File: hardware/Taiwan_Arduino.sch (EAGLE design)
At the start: 43 parts, among them J1 AVR_SPI_PRG_62X3_LOCK, T2 2N, U1 ATMEGA328P_PDIP, Y2 16mhz

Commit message: ver 1.0
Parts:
- removed R7: 1M, SparkFun-Resistors:RESISTORPTH-1/4W
- removed TP5: TEST-POINT, SparkFun-Passives:TEST-POINT
- added D3: 3.3V, _JJG-parts:DIODE-VERTDIODE_SM_VERT
- added JP1: Battery, SparkFun-Connectors:M02PTH
- C10, C13, C5, C8: device SparkFun-Capacitors:CAPPTH -> SparkFun-Capacitors:CAPPTH1
- C2: value 0.1uf -> 104; device SparkFun-Capacitors:CAPPTH -> SparkFun-Capacitors:CAPPTH1
- JP3: value M02JST-PTH-VERT -> M021X02_NO_SILK; device SparkFun-Connectors:M02JST-PTH-VERT -> SparkFun-Connectors:M021X02_NO_SILK
- R1: value (none) -> 10
- R9: device SparkFun-Resistors:RESISTORPTH-1/4W -> SparkFun-Resistors:RESISTORPTH-1/4W-VERT
- T2: value 2N -> 2N2222
- U2: value SPI_FLASH-X25XX -> SPI_FLASH
- renumbered U$1 to U2
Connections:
- removed net N$27: R7.2, TP5.1, U1.PD4(XCK/T0)
- new net N$18: D3.A, JP1.2
- net +5V: now also D3.C
- net GND: now also JP1.1
- net N$11: now also U1.PC3(ADC3); no longer R7.1, U1.PC2(ADC2)
- net N$28: now also U1.PB2(SS/OC1B); no longer U1.PB0(ICP)
- net N$3: now also U1.PB0(ICP); no longer U1.PB2(SS/OC1B)
- net N$5: now also U1.PC2(ADC2); no longer U1.PC1(ADC1)
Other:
- moved on the sheet: JP3, TP1, TP9

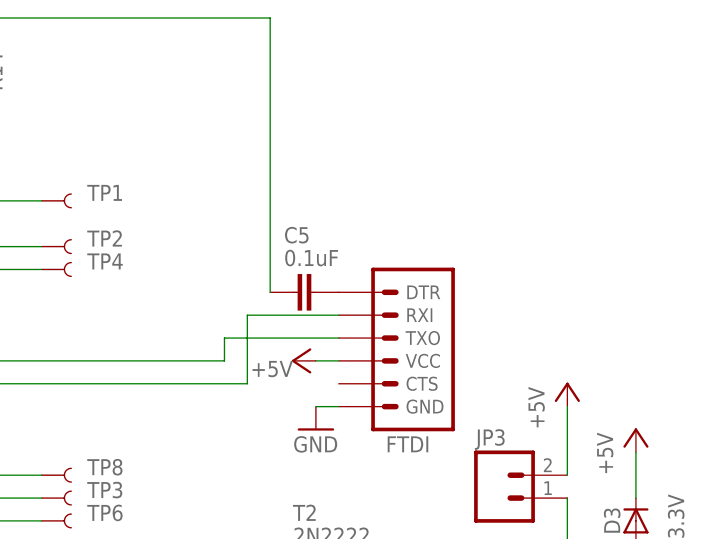
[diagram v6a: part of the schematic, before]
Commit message: add tag on FTDI port
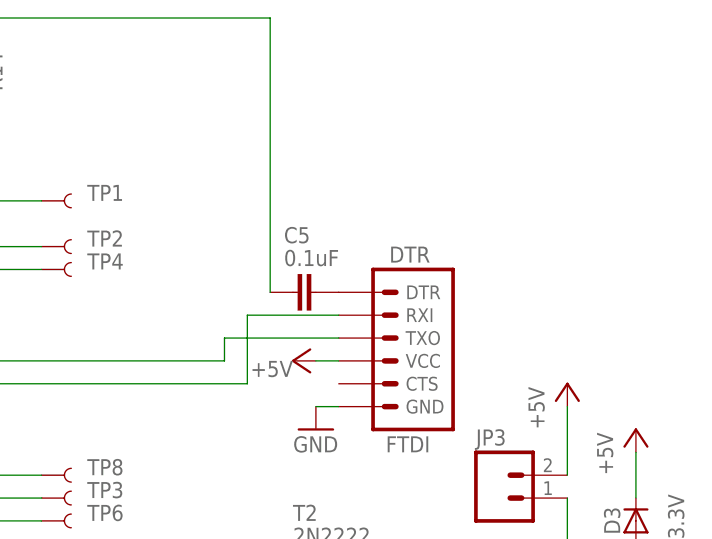
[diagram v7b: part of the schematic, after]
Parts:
- FTDI: value (none) -> DTR
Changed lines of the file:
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@@
 <part name="TP8" library="SparkFun-Passives" deviceset="TEST-POINT" device=""/>
 <part name="TP9" library="SparkFun-Passives" deviceset="TEST-POINT" device=""/>
-<part name="FTDI" library="SparkFun-Connectors" deviceset="ARDUINO_SERIAL_PROGRAM" device="LOCK"/>
+<part name="FTDI" library="SparkFun-Connectors" deviceset="ARDUINO_SERIAL_PROGRAM" device="LOCK" value="DTR"/>
 <part name="GND3" library="supply1" deviceset="GND" device=""/>
 <part name="P+1" library="supply1" deviceset="+5V" device=""/>

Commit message: add FTDI pin labels
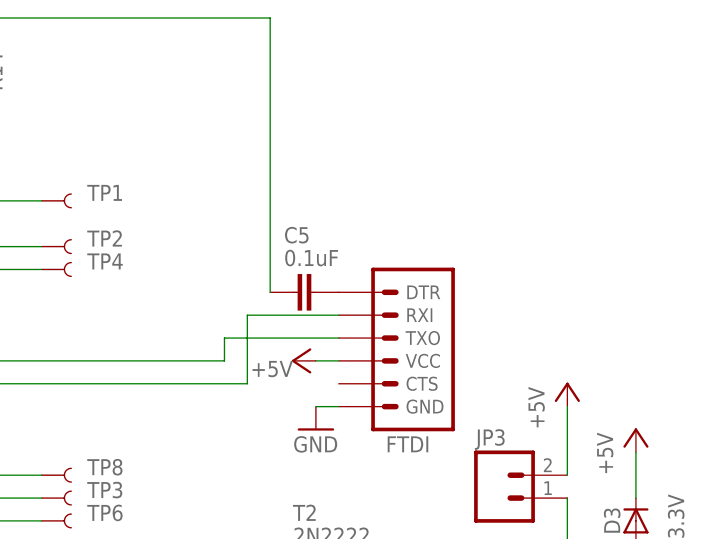
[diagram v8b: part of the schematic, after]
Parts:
- FTDI: value DTR -> (none)
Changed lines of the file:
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@@
 <?xml version="1.0" encoding="utf-8"?>
 <!DOCTYPE eagle SYSTEM "eagle.dtd">
-<eagle version="7.4.0">
+<eagle version="7.2.0">
 <drawing>
 <settings>
@@
 <grid distance="0.1" unitdist="inch" unit="inch" style="lines" multiple="1" display="no" altdistance="0.01" altunitdist="inch" altunit="inch"/>
 <layers>
-<layer number="1" name="Top" color="4" fill="1" visible="no" active="no"/>
-<layer number="16" name="Bottom" color="1" fill="1" visible="no" active="no"/>
-<layer number="17" name="Pads" color="2" fill="1" visible="no" active="no"/>
-<layer number="18" name="Vias" color="2" fill="1" visible="no" active="no"/>
-<layer number="19" name="Unrouted" color="6" fill="1" visible="no" active="no"/>
-<layer number="20" name="Dimension" color="15" fill="1" visible="no" active="no"/>
-<layer number="21" name="tPlace" color="7" fill="1" visible="no" active="no"/>
-<layer number="22" name="bPlace" color="7" fill="1" visible="no" active="no"/>
-<layer number="23" name="tOrigins" color="15" fill="1" visible="no" active="no"/>
-<layer number="24" name="bOrigins" color="15" fill="1" visible="no" active="no"/>
-<layer number="25" name="tNames" color="7" fill="1" visible="no" active="no"/>
-<layer number="26" name="bNames" color="7" fill="1" visible="no" active="no"/>
-<layer number="27" name="tValues" color="7" fill="1" visible="no" active="no"/>
-<layer number="28" name="bValues" color="7" fill="1" visible="no" active="no"/>
+<layer number="1" name="Top" color="4" fill="1" visible="yes" active="no"/>
+<layer number="16" name="Bottom" color="1" fill="1" visible="yes" active="no"/>
+<layer number="17" name="Pads" color="2" fill="1" visible="yes" active="no"/>
+<layer number="18" name="Vias" color="2" fill="1" visible="yes" active="no"/>
+<layer number="19" name="Unrouted" color="6" fill="1" visible="yes" active="no"/>
+<layer number="20" name="Dimension" color="15" fill="1" visible="yes" active="no"/>
+<layer number="21" name="tPlace" color="7" fill="1" visible="yes" active="no"/>
+<layer number="22" name="bPlace" color="7" fill="1" visible="yes" active="no"/>
+<layer number="23" name="tOrigins" color="15" fill="1" visible="yes" active="no"/>
+<layer number="24" name="bOrigins" color="15" fill="1" visible="yes" active="no"/>
+<layer number="25" name="tNames" color="7" fill="1" visible="yes" active="no"/>
+<layer number="26" name="bNames" color="7" fill="1" visible="yes" active="no"/>
+<layer number="27" name="tValues" color="7" fill="1" visible="yes" active="no"/>
+<layer number="28" name="bValues" color="7" fill="1" visible="yes" active="no"/>
 <layer number="29" name="tStop" color="7" fill="3" visible="no" active="no"/>
 <layer number="30" name="bStop" color="7" fill="6" visible="no" active="no"/>
@@
 <layer number="35" name="tGlue" color="7" fill="4" visible="no" active="no"/>
 <layer number="36" name="bGlue" color="7" fill="5" visible="no" active="no"/>
-<layer number="37" name="tTest" color="7" fill="1" visible="no" active="no"/>
-<layer number="38" name="bTest" color="7" fill="1" visible="no" active="no"/>
+<layer number="37" name="tTest" color="7" fill="1" visible="yes" active="no"/>
+<layer number="38" name="bTest" color="7" fill="1" visible="yes" active="no"/>
 <layer number="39" name="tKeepout" color="4" fill="11" visible="no" active="no"/>
 <layer number="40" name="bKeepout" color="1" fill="11" visible="no" active="no"/>
@@
 <layer number="44" name="Drills" color="7" fill="1" visible="no" active="no"/>
 <layer number="45" name="Holes" color="7" fill="1" visible="no" active="no"/>
-<layer number="46" name="Milling" color="3" fill="1" visible="no" active="no"/>
-<layer number="47" name="Measures" color="7" fill="1" visible="no" active="no"/>
-<layer number="48" name="Document" color="7" fill="1" visible="no" active="no"/>
-<layer number="49" name="Reference" color="7" fill="1" visible="no" active="no"/>
-<layer number="50" name="dxf" color="7" fill="1" visible="no" active="no"/>
-<layer number="51" name="tDocu" color="7" fill="1" visible="no" active="no"/>
-<layer number="52" name="bDocu" color="7" fill="1" visible="no" active="no"/>
-<layer number="53" name="tGND_GNDA" color="7" fill="9" visible="no" active="no"/>
-<layer number="54" name="bGND_GNDA" color="1" fill="9" visible="no" active="no"/>
-<layer number="56" name="wert" color="7" fill="1" visible="no" active="no"/>
-<layer number="57" name="tCAD" color="7" fill="1" visible="no" active="no"/>
-<layer number="59" name="tCarbon" color="7" fill="1" visible="no" active="no"/>
-<layer number="60" name="bCarbon" color="7" fill="1" visible="no" active="no"/>
+<layer number="46" name="Milling" color="3" fill="1" visible="yes" active="no"/>
+<layer number="47" name="Measures" color="7" fill="1" visible="yes" active="no"/>
+<layer number="48" name="Document" color="7" fill="1" visible="yes" active="no"/>
+<layer number="49" name="Reference" color="7" fill="1" visible="yes" active="no"/>
+<layer number="50" name="dxf" color="7" fill="1" visible="yes" active="no"/>
+<layer number="51" name="tDocu" color="7" fill="1" visible="yes" active="no"/>
+<layer number="52" name="bDocu" color="7" fill="1" visible="yes" active="no"/>
+<layer number="53" name="tGND_GNDA" color="7" fill="9" visible="yes" active="no"/>
+<layer number="54" name="bGND_GNDA" color="1" fill="9" visible="yes" active="no"/>
+<layer number="56" name="wert" color="7" fill="1" visible="yes" active="no"/>
+<layer number="57" name="tCAD" color="7" fill="1" visible="yes" active="no"/>
+<layer number="59" name="tCarbon" color="7" fill="1" visible="yes" active="no"/>
+<layer number="60" name="bCarbon" color="7" fill="1" visible="yes" active="no"/>
 <layer number="90" name="Modules" color="5" fill="1" visible="yes" active="yes"/>
 <layer number="91" name="Nets" color="2" fill="1" visible="yes" active="yes"/>
@@
 <part name="TP8" library="SparkFun-Passives" deviceset="TEST-POINT" device=""/>
 <part name="TP9" library="SparkFun-Passives" deviceset="TEST-POINT" device=""/>
-<part name="FTDI" library="SparkFun-Connectors" deviceset="ARDUINO_SERIAL_PROGRAM" device="LOCK" value="DTR"/>
+<part name="FTDI" library="SparkFun-Connectors" deviceset="ARDUINO_SERIAL_PROGRAM" device="LOCK"/>
 <part name="GND3" library="supply1" deviceset="GND" device=""/>
 <part name="P+1" library="supply1" deviceset="+5V" device=""/>
